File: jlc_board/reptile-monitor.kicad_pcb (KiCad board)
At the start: 4 copper layers, 38.1 x 38.1 mm, 33 parts, among them J1 AudioJack4_SwitchR1, J2 AudioJack4_SwitchR1, J3 PWR CONN, J4 UART, J6 18-Lead FPC 0.5 mm - Vertical, Q1 2SC1741, SW1 RESET, U1 AP2112M-3.3, U2 TCA4307DGKR

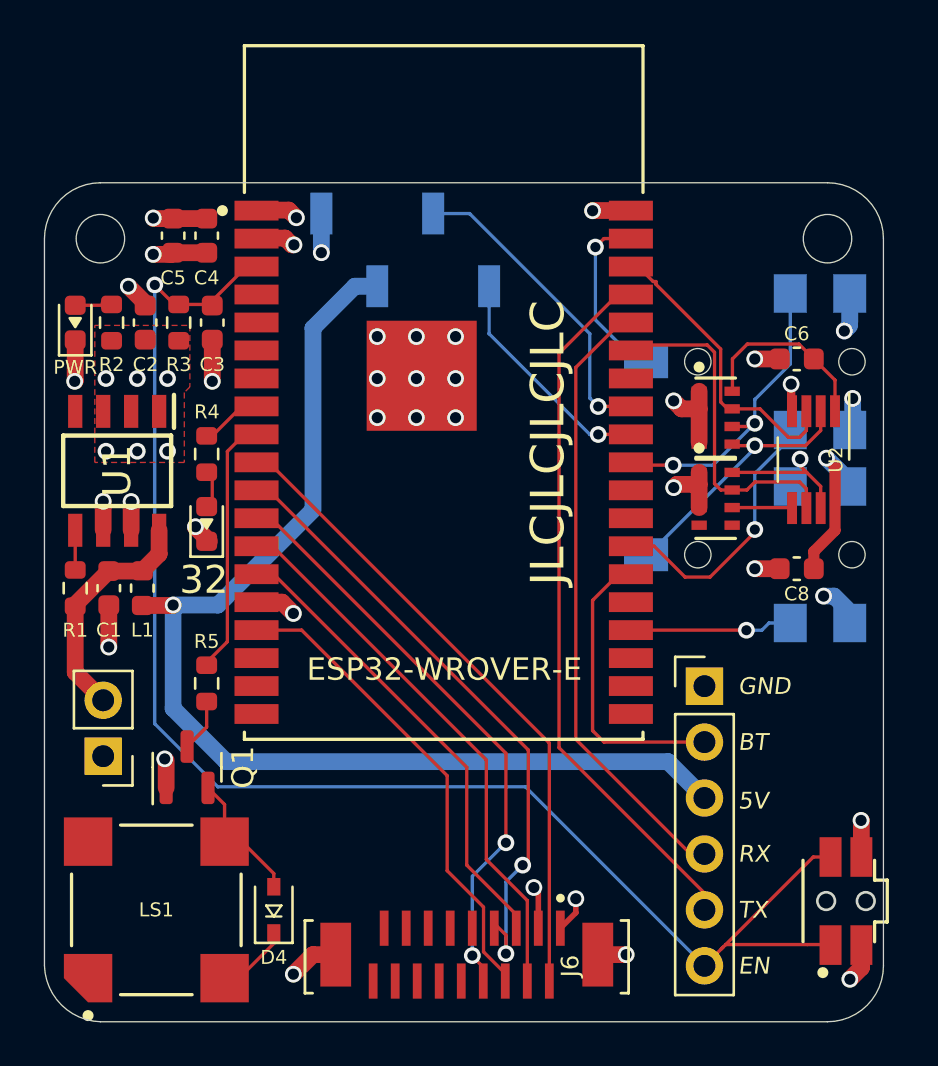
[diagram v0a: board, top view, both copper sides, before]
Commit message: Eliminate I2C Chip & move stemma qt connector to top
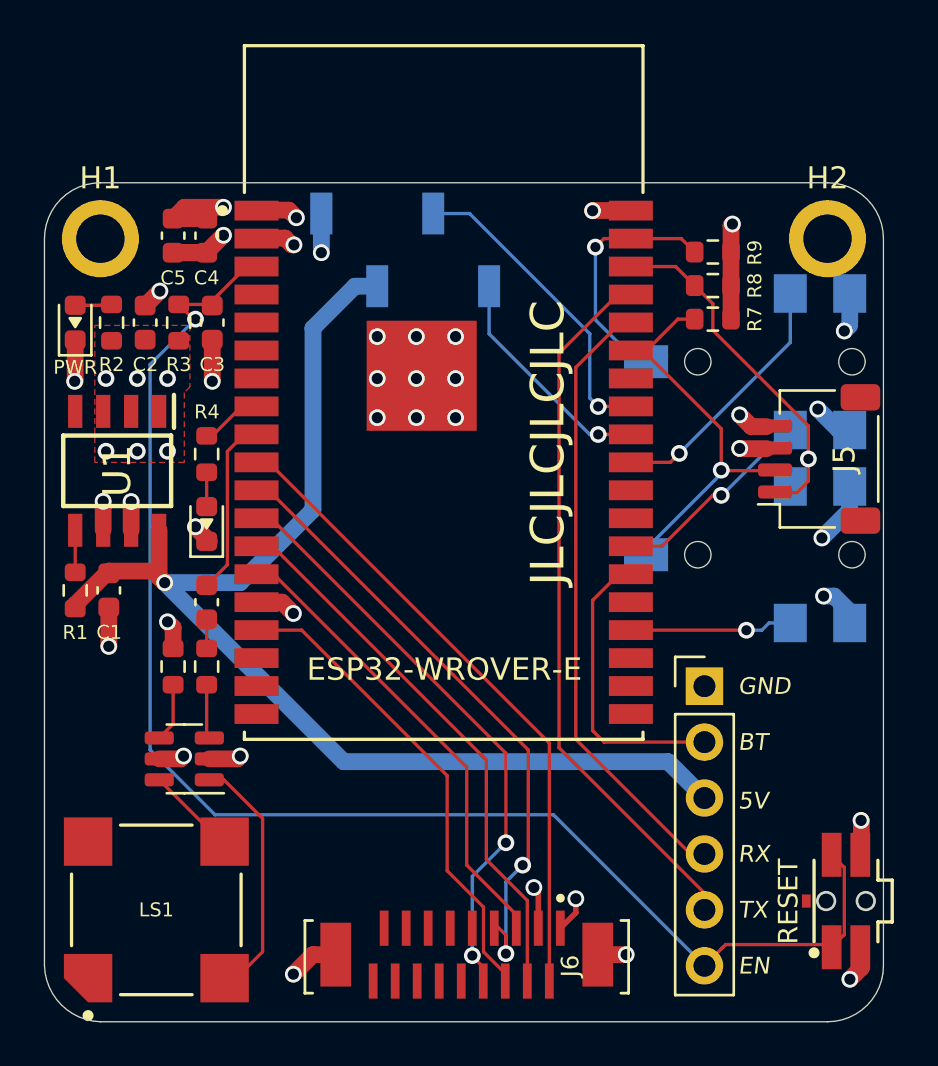
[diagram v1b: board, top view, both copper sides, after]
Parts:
- removed C8: 100n, reptile-monitor:C_0603_1608Metric
- removed D4: BAS316, reptile-monitor:D_SOD-323
- removed L1: 360 m, reptile-monitor:L_0603_1608Metric
- removed Q1: 2SC1741, Package_TO_SOT_SMD:SOT-23
- removed RN1, RN2: 10k, reptile-monitor:Panasonic-EXB-V8V103JV-0
- removed TP1: TestPoint_2Pole, Connector_PinHeader_2.54mm:PinHeader_1x02_P2.54mm_Vertical
- added J5: I2C, reptile-monitor:JST_SH_SM04B-SRSS-TB_1x04-1MP_P1.00mm_Horizontal, F.Cu at (151.3, 90.3)
- added R6: 47k, reptile-monitor:R_0603_1608Metric, F.Cu at (123.5, 99.7)
- added R7: 10k, reptile-monitor:R_0603_1608Metric, F.Cu at (146.5, 83.9)
- added R8: 10k, reptile-monitor:R_0603_1608Metric, F.Cu at (146.5, 82.4)
- added R9: 10k, reptile-monitor:R_0603_1608Metric, F.Cu at (146.5, 80.9)
- C6: value 100n -> 1u
- H1, H2: footprint MountingHole:MountingHole_2.2mm_M2_ISO7380 -> MountingHole:MountingHole_2.2mm_M2_ISO7380_Pad
- R5: value 1k -> 10k
- SW1: footprint reptile-monitor:AlpsAlpine_SKSCPD -> reptile-monitor:Panasonic-EVQ-P7A01P
- U2: value TCA4307DGKR -> PAM8301; footprint reptile-monitor:VSSOP-8_3.0x3.0mm_P0.65mm -> Package_TO_SOT_SMD:SOT-23-6
- moved U2 31.6 mm to (122.5, 103.9), turned to 180 degrees
- moved C6 29.0 mm to (123.5, 96.8), turned to 90 degrees
- moved R5 1.70 mm to (122.0, 99.7), turned to 90 degrees
- moved WAFFLE 0.38 mm to (132.2, 98.0)
- moved C1 0.10 mm to (119.1, 96.2)
- moved R1 0.10 mm to (117.6, 96.2)
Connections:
- C1 pad 1: /PWR_IN -> +5V
- C6 pad 1: /U2_EN -> Net-(C6-Pad1)
- C6 pad 2: GND -> SPK
- J1 pad 2: SCL_BUFFERED -> SDA0
- J1 pad 3: SDA_BUFFERED -> SCL0
- J6 pad 10: (no net) -> unconnected-(J6-Pad10)
- J6 pad 11: (no net) -> unconnected-(J6-Pad11)
- J6 pad 12: (no net) -> unconnected-(J6-Pad12)
- J6 pad 13: (no net) -> unconnected-(J6-Pad13)
- J6 pad 14: (no net) -> unconnected-(J6-Pad14)
- J6 pad 15: (no net) -> unconnected-(J6-Pad15)
- J6 pad 16: (no net) -> unconnected-(J6-Pad16)
- J6 pad 17: (no net) -> unconnected-(J6-Pad17)
- J6 pad 18: (no net) -> unconnected-(J6-Pad18)
- J6 pad 9: (no net) -> IO28
- LS1 pad 1: (no net) -> unconnected-(LS1-Pad1)
- LS1 pad 2: (no net) -> unconnected-(LS1-Pad2)
- LS1 pad 3: Net-(D4-Pad1) -> Net-(U2-Pad1)
- LS1 pad 4: Net-(D4-Pad2) -> Net-(U2-Pad6)
- MD1 pad 17: (no net) -> unconnected-(MD1-Pad17)
- MD1 pad 18: (no net) -> unconnected-(MD1-Pad18)
- MD1 pad 19: (no net) -> unconnected-(MD1-Pad19)
- MD1 pad 20: (no net) -> unconnected-(MD1-Pad20)
- MD1 pad 21: (no net) -> unconnected-(MD1-Pad21)
- MD1 pad 22: (no net) -> unconnected-(MD1-Pad22)
- MD1 pad 24: (no net) -> /IO2
- MD1 pad 27: (no net) -> unconnected-(MD1-Pad27)
- MD1 pad 28: (no net) -> unconnected-(MD1-Pad28)
- MD1 pad 32: (no net) -> unconnected-(MD1-Pad32)
- MD1 pad 4: (no net) -> unconnected-(MD1-Pad4)
- MD1 pad 5: (no net) -> unconnected-(MD1-Pad5)
- MD1 pad 6: (no net) -> unconnected-(MD1-Pad6)
- MD1 pad 7: (no net) -> unconnected-(MD1-Pad7)
- R1 pad 2: /PWR_IN -> +5V
- R5 pad 1: SPK -> Net-(R5-Pad1)
- R5 pad 2: Net-(Q1-Pad3) -> +3V3
- U1 pad 4: (no net) -> unconnected-(U1-Pad4)
- U1 pad 8: /PWR_IN -> +5V
- U2 pad 1: /U2_EN -> Net-(U2-Pad1)
- U2 pad 2: SCL_BUFFERED -> GND
- U2 pad 3: SCL0 -> Net-(R6-Pad1)
- U2 pad 4: GND -> Net-(R5-Pad1)
- U2 pad 5: /U2_RDY -> +3V3
- U2 pad 6: SDA0 -> Net-(U2-Pad6)
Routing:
- net SCL_BUFFERED: track 11.9 -> 0.00 mm, vias 1 -> 0
- net Net-(U2-Pad1): track 0.00 -> 11.4 mm
- net /PWR_IN: track 10.7 -> 0.00 mm
- net /U2_EN: track 8.50 -> 0.00 mm
- net SDA_BUFFERED: track 7.30 -> 0.00 mm, vias 1 -> 0
- net Net-(D4-Pad2): track 5.40 -> 0.00 mm
- net Net-(U2-Pad6): track 0.00 -> 4.13 mm
- net +5V: track 52.0 -> 56.1 mm
- net SCL0: track 13.2 -> 17.2 mm, vias 0 -> 1
- net SPK: track 11.1 -> 7.57 mm
- net SDA0: track 15.0 -> 18.3 mm, vias 0 -> 1
- net IO23: track 7.77 -> 10.9 mm
- net /U2_RDY: track 2.87 -> 0.00 mm
- net Net-(D4-Pad1): track 2.70 -> 0.00 mm
- net Net-(R5-Pad1): track 0.00 -> 2.68 mm
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
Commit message: change blu led to 1k resistor so it's brighter
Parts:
- H1: value MountingHole -> GND
- moved WAFFLE 0.99 mm to (132.0, 99.0)
- moved J1 0.86 mm to (154.3, 95.5)
- moved J5 0.86 mm to (151.3, 91.1)
- moved J2 0.86 mm to (154.3, 86.7)
- moved R7 0.86 mm to (146.5, 84.8)
- moved R8 0.86 mm to (146.5, 83.3)
- moved R9 0.86 mm to (146.5, 81.7)
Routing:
- net IO23: track 10.9 -> 12.4 mm
- net SDA0: track 18.3 -> 18.8 mm
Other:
- outline, holes or cut-outs redrawn
- board text added: "Rev. 4.5 Dec 2021"
- board text removed: "Rev. 4.5 Oct 2021"

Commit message: rev5
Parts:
- removed C6: 1u, reptile-monitor:C_0603_1608Metric
- removed J5: I2C, reptile-monitor:JST_SH_SM04B-SRSS-TB_1x04-1MP_P1.00mm_Horizontal
- removed R6: 47k, reptile-monitor:R_0603_1608Metric
- removed R7, R8, R9: 10k, reptile-monitor:R_0603_1608Metric
- removed U2: PAM8301, Package_TO_SOT_SMD:SOT-23-6
- added D3: 1N4007, reptile-monitor:D_SOD-323, F.Cu at (126.7, 108.0)
- added D4: 1N4007, reptile-monitor:D_SOD-323, F.Cu at (121.4, 96.5)
- added D5: 1N4007, reptile-monitor:D_SOD-323, F.Cu at (123.3, 96.5)
- added Q1: Q_NPN_BEC, reptile-monitor:SOT-23, F.Cu at (118.7, 104.1)
- added RN1: 10k, reptile-monitor:Panasonic-EXB-V8V103JV-0, F.Cu at (145.7, 90.9)
- H1: value GND -> MountingHole
- R4: value 10k -> 1k
- R5: value 10k -> 1K
- moved R5 4.46 mm to (121.4, 104.1)
- moved D2 0.43 mm to (123.4, 92.8)
- moved R4 0.43 mm to (123.4, 89.6)
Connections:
- net IO25 renamed BK_LT
- net IO26 renamed TFT_DC
- net IO27 renamed TFT_RST
- net IO32 renamed /LED
- J1 pad 2: SDA0 -> DS_DATA
- J1 pad 3: SCL0 -> DS_0
- J1 pad 5: IO15 -> unconnected-(J1-Pad5)
- J2 pad 2: IO23 -> SDA0
- J2 pad 3: IO5 -> SCL0
- J2 pad 5: IO4 -> unconnected-(J2-Pad5)
- J3 pad 2: +5V -> Net-(J3-Pad2)
- J4 pad 3: +5V -> Net-(J4-Pad3)
- J6 pad 10: unconnected-(J6-Pad10) -> SD_CS
- J6 pad 9: IO28 -> TFT_CS
- LS1 pad 3: Net-(U2-Pad1) -> VDD
- MD1 pad 23: IO15 -> TFT_CS
- MD1 pad 24: /IO2 -> SD_CS
- MD1 pad 26: IO4 -> DS_DATA
- MD1 pad 29: IO5 -> unconnected-(MD1-Pad29)
- MD1 pad 37: IO23 -> DS_0
- MD1 pad 9: SPK -> BUZZER
- R5 pad 1: Net-(R5-Pad1) -> BUZZER
- R5 pad 2: +3V3 -> Net-(Q1-Pad1)
- U1 pad 2: +3V3 -> unconnected-(U1-Pad2)
- U1 pad 3: +3V3 -> unconnected-(U1-Pad3)
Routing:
- net +5V: track 56.0 -> 8.29 mm, vias 1 -> 0
- net Net-(J4-Pad3): track 0.00 -> 29.8 mm, vias 0 -> 1
- net SD_CS: track 0.00 -> 24.5 mm, vias 0 -> 2
- net Net-(J3-Pad2): track 0.00 -> 22.0 mm, vias 0 -> 1
- net TFT_CS: track 0.00 -> 20.5 mm, vias 0 -> 2
- net DS_0: track 0.00 -> 20.2 mm, vias 0 -> 2
- net BUZZER: track 0.00 -> 18.9 mm
- net IO23: track 12.4 -> 0.00 mm, vias 1 -> 0
- net Net-(U2-Pad1): track 11.4 -> 0.00 mm
- net IO5: track 11.4 -> 0.00 mm, vias 1 -> 0
- net SDA0: track 18.8 -> 8.59 mm
- net IO4: track 9.07 -> 0.00 mm, vias 1 -> 0
- net DS_DATA: track 0.00 -> 8.74 mm, vias 0 -> 1
- net SPK: track 7.57 -> 0.00 mm
- net IO15: track 7.47 -> 0.00 mm, vias 1 -> 0
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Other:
- board text added: "BOOT"
- board text added: "Rev. 5 Feb 2022"
- board text removed: "BT"
- board text removed: "Rev. 4.5 Dec 2021"
